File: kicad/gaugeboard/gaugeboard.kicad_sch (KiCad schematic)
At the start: 22 parts, among them J1 LOOM from main board (4-wire 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, J2 HB1 half-bridge #1 (on beam):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, J3 HB2 half-bridge #2 (on beam):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, U1 3.3 V LDO: LP2950-N 3.3 V (TO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, U2 Adafruit ADS122C04 #1 (I2C 0x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, U3 Adafruit ADS122C04 #2 (addres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

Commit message: Gauge board: add pass-through loom output header (J2)
Second 1x4 header wired in parallel with the loom input (GND, +5V, SDA, SCL)
so another I2C board can be daisy-chained. Gauge headers renumbered J3/J4;
docs updated.

Co-Authored-By: Claude Sonnet 5.5 <noreply@anthropic.com>
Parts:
- removed J2: HB1 half-bridge #1 (on beam): V, SIG, GND, Connector_PinHeader_2.54mm:PinHeader_1x03_P2.54mm_Vertical, symbol HastaDAQ:Header1x03_VpSIGpGND
- added J2: LOOM OUT (pass-through, paralleled with J1): GND,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, Connector_PinHeader_2.54mm:PinHeader_1x04_P2.54mm_Vertical, symbol HastaDAQ:Header1x04_GNDp5VpSDApSCL
- added J4: HB2 half-bridge #2 (on beam): V, SIG, GND, Connector_PinHeader_2.54mm:PinHeader_1x03_P2.54mm_Vertical, symbol HastaDAQ:Header1x03_VpSIGpGND
- J3: value HB2 half-bridge #2 (on beam): V, SIG, GND -> HB1 half-bridge #1 (on beam): V, SIG, GND
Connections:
- net +3V3: now also J4.1 (V)
- net +5V: now also J2.2 (5V)
- net ADS1_SIG: now also J3.2 (SIG)
- net ADS2_SIG: now also J4.2 (SIG); no longer J3.2 (SIG)
- net GND: now also J2.1 (GND), J4.3 (GND)
- net SCL: now also J2.4 (SCL)
- net SDA: now also J2.3 (SDA)
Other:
- note added: "Second 1x4 header wired straight to the loom: daisy-chains another I2C board (+5V, 3.3 V logic)."

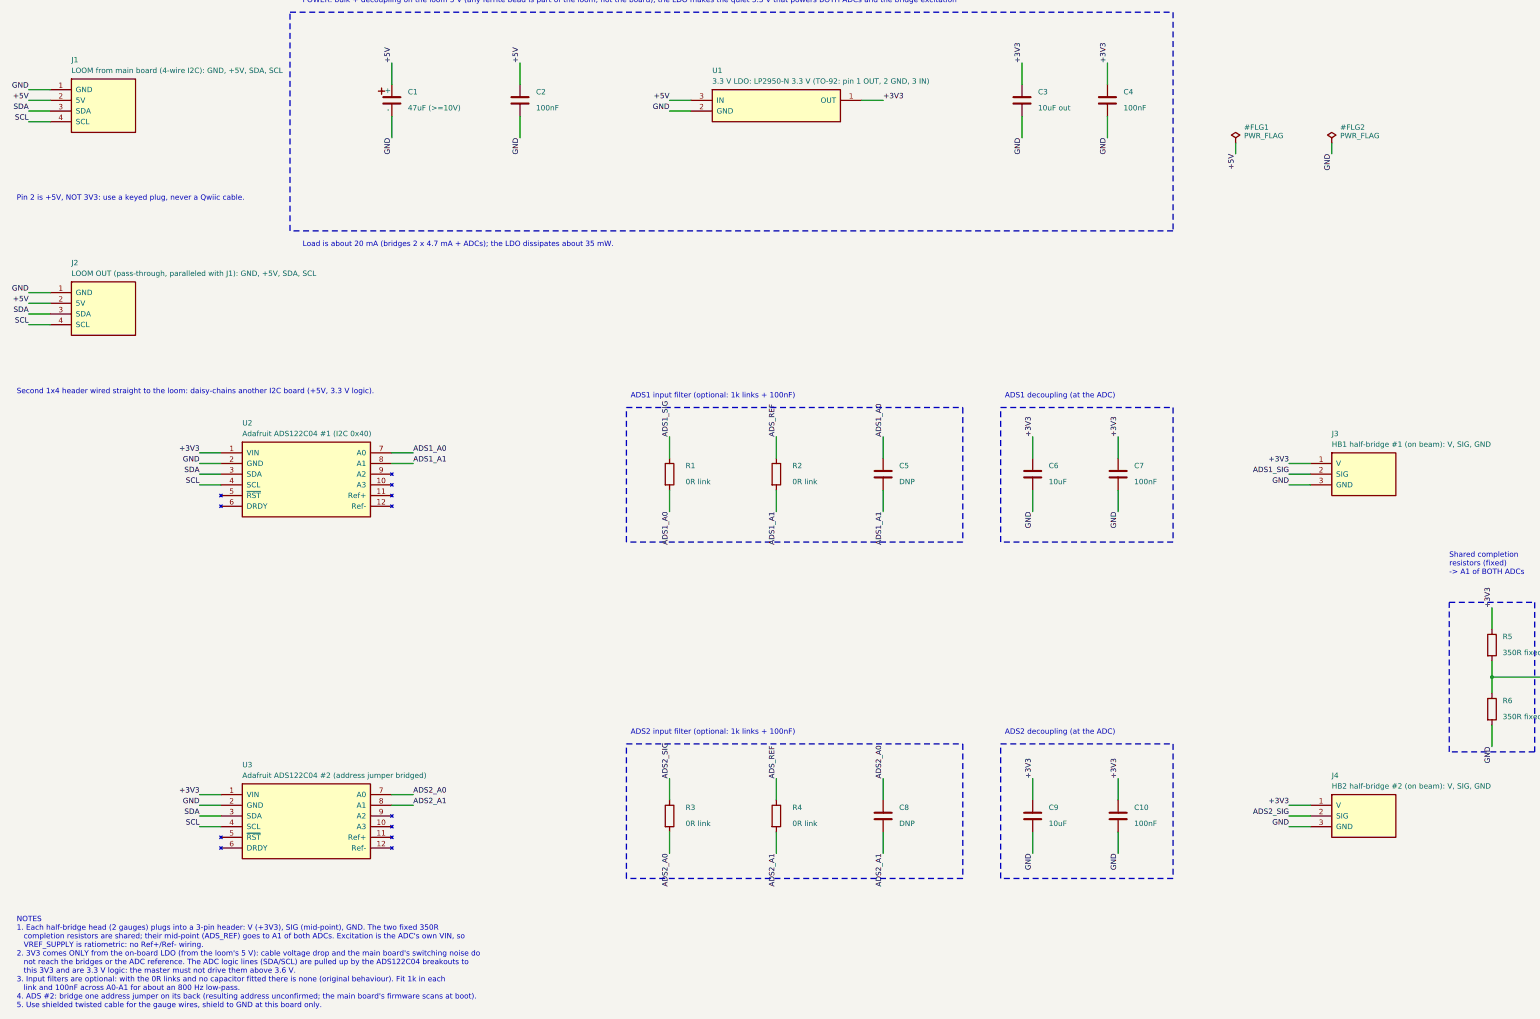
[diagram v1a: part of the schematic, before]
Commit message: Schematics: fuse removed, plain headers, real parts chosen; gauge board LDO/caps; hand-off docs
- Main board: no fuse (+12V straight from the supply connector), every connector a
  plain 0.1 in header, plain test pads, FOD817A opto, chosen capacitor footprints
- Gauge board: MCP1700-3302E/TO LDO (pin 1 GND, 2 VIN, 3 VOUT), tantalum output cap,
  Vishay K-series 100 nF with 2.5 mm pitch, DNP flags on the filter caps, test points,
  pass-through loom header, redundant ADC decoupling removed
- Docs: PCB_BRIEF.md/PCB_BRIEF_GAUGE.md rewritten with a status and hand-off section,
  new PARTS_TO_SELECT.md (RS numbers, dimensions, open items), README updated,
  BabyBuck EN and ADS122C04 pull-up/address facts recorded from the data sheets

Co-Authored-By: Claude Sonnet 5.5 <noreply@anthropic.com>
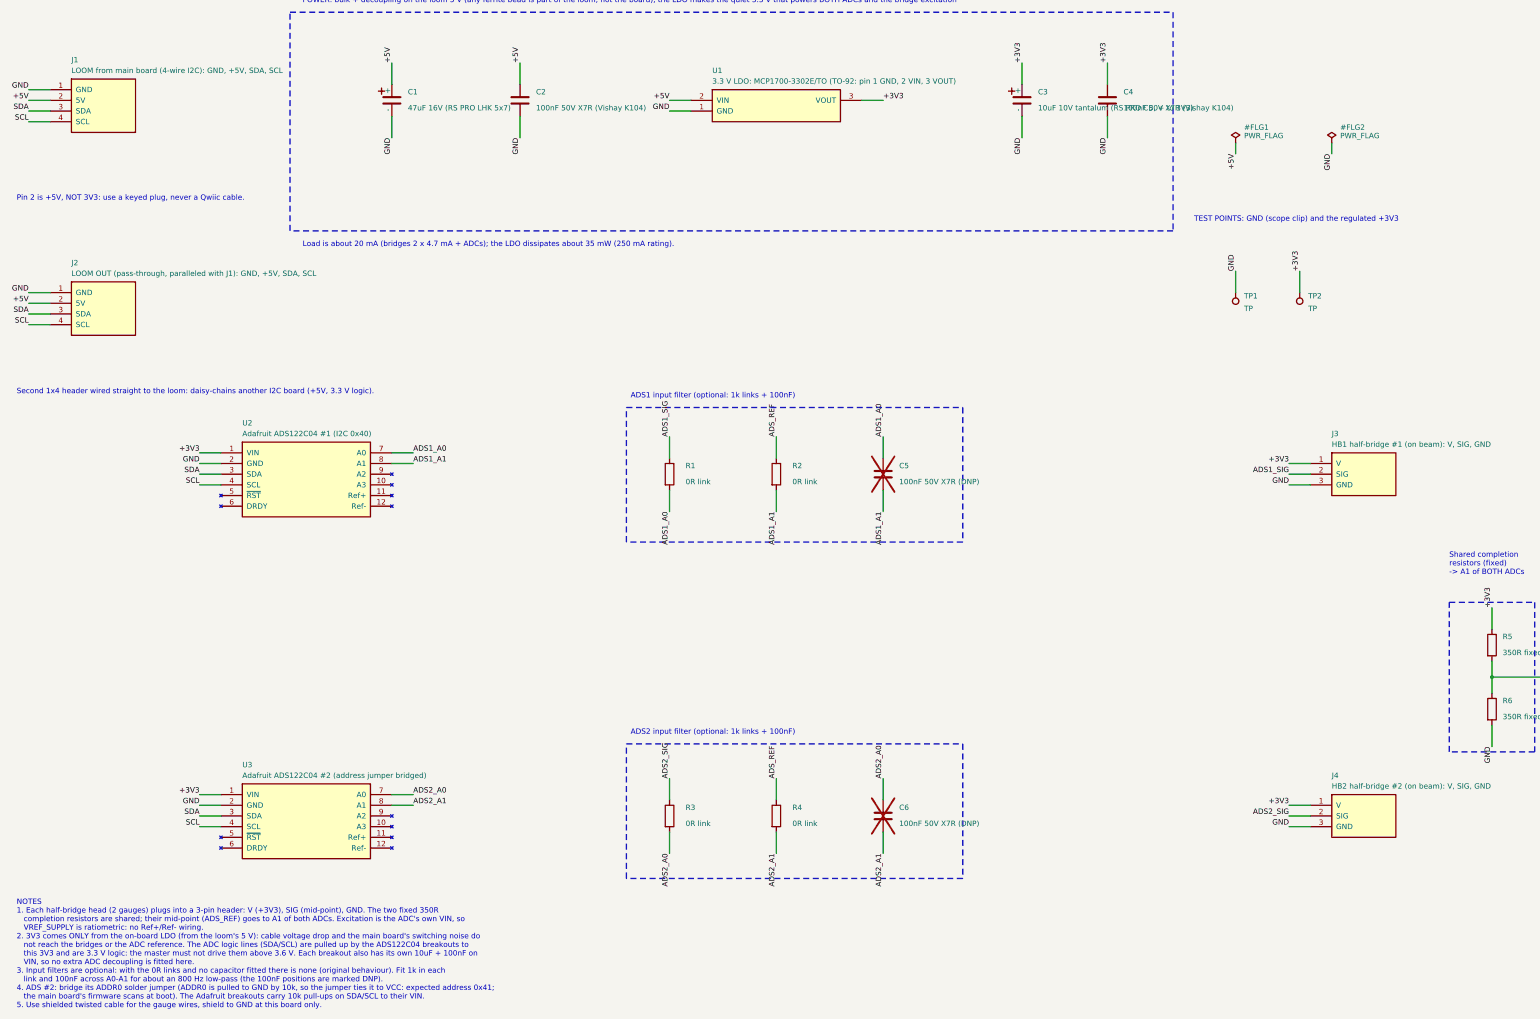
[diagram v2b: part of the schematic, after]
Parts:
- removed C10, C7: 100nF, Capacitor_THT:C_Disc_D5.0mm_W2.5mm_P5.00mm, symbol HastaDAQ:C
- removed C3: 10uF out, Capacitor_THT:C_Rect_L7.2mm_W3.5mm_P5.00mm, symbol HastaDAQ:C
- removed C8: DNP, Capacitor_THT:C_Disc_D5.0mm_W2.5mm_P5.00mm, symbol HastaDAQ:C
- removed C9: 10uF, Capacitor_THT:C_Rect_L7.2mm_W3.5mm_P5.00mm, symbol HastaDAQ:C
- added C3: 10uF 10V tantalum (RS PRO CB, + to 3V3), Capacitor_THT:CP_Radial_D5.0mm_P2.50mm, symbol HastaDAQ:C_Polarized
- added TP1, TP2: TP, TestPoint:TestPoint_Pad_D2.0mm, symbol HastaDAQ:TestPoint
- C1: value 47uF (>=10V) -> 47uF 16V (RS PRO LHK 5x7)
- C2, C4: value 100nF -> 100nF 50V X7R (Vishay K104); footprint Capacitor_THT:C_Disc_D5.0mm_W2.5mm_P5.00mm -> Capacitor_THT:C_Rect_L4.0mm_W2.5mm_P2.50mm
- C5: value DNP -> 100nF 50V X7R (DNP); footprint Capacitor_THT:C_Disc_D5.0mm_W2.5mm_P5.00mm -> Capacitor_THT:C_Rect_L4.0mm_W2.5mm_P2.50mm; now not fitted
- C6: value 10uF -> 100nF 50V X7R (DNP); footprint Capacitor_THT:C_Rect_L7.2mm_W3.5mm_P5.00mm -> Capacitor_THT:C_Rect_L4.0mm_W2.5mm_P2.50mm; now not fitted
- U1: value 3.3 V LDO: LP2950-N 3.3 V (TO-92: pin 1 OUT, 2 GND, 3 IN) -> 3.3 V LDO: MCP1700-3302E/TO (TO-92: pin 1 GND, 2 VIN, 3 VOUT)
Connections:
- net +3V3: now also U1.3 (VOUT), C3.1 (+), TP2.1; no longer C6.1, U1.1 (OUT)
- net +5V: now also U1.2 (VIN); no longer U1.3 (IN)
- net ADS2_A0: now also C6.1
- net ADS2_A1: now also C6.2
- net GND: now also U1.1 (GND), C3.2 (-), TP1.1; no longer C6.2, U1.2 (GND)
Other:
- note added: "Load is about 20 mA (bridges 2 x 4.7 mA + ADCs); the LDO dissipates about 35 mW (250 mA rating)."
- note added: "TEST POINTS: GND (scope clip) and the regulated +3V3"
- note removed: "ADS1 decoupling (at the ADC)"
- note removed: "ADS2 decoupling (at the ADC)"
- note removed: "Load is about 20 mA (bridges 2 x 4.7 mA + ADCs); the LDO dissipates about 35 mW."

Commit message: Gauge board PCB laid out, routed and sent to PCBWay; layout scripts, docs and hand-off README
- Gauge board: J3/J4 become 2x3 headers (V V / SIG SIG / GND GND) in generate_gauge_sch.py;
  republished release 20261026-2252-rev-a (replaces 20261026-1734-rev-a) with the laid-out
  gaugeboard.kicad_pcb and the PCBWay fab files (fab/gaugeboard_gerbers.zip).
- kicad/tools/layout/: export_fab.py, tidy_silk.py, remove_pads.py, set_pcbway_rules.py plus
  board-specific placement/routing/length-check records for the gauge board, with a README.
- kicad/README.md: workflow, tools, gotchas, status, as-built gauge board, next steps for the main board.
- docs: PCB_BRIEF_GAUGE.md updated to the as-built layout, PARTS_TO_SELECT.md and README.md to match.
- Not committed: the nested KiCad .history folder in the release (local editor history).

Co-Authored-By: Claude Sonnet 5.5 <noreply@anthropic.com>
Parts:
- removed J3: HB1 half-bridge #1 (on beam): V, SIG, GND, Connector_PinHeader_2.54mm:PinHeader_1x03_P2.54mm_Vertical, symbol HastaDAQ:Header1x03_VpSIGpGND
- removed J4: HB2 half-bridge #2 (on beam): V, SIG, GND, Connector_PinHeader_2.54mm:PinHeader_1x03_P2.54mm_Vertical, symbol HastaDAQ:Header1x03_VpSIGpGND
- added J3: HB1 half-bridge #1 (on beam), 2x3: V V / SIG SIG 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, Connector_PinHeader_2.54mm:PinHeader_2x03_P2.54mm_Vertical, symbol HastaDAQ:Header2x03_VpVpSIGpSIGpGNDpGND
- added J4: HB2 half-bridge #2 (on beam), 2x3: V V / SIG SIG 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, Connector_PinHeader_2.54mm:PinHeader_2x03_P2.54mm_Vertical, symbol HastaDAQ:Header2x03_VpVpSIGpSIGpGNDpGND
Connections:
- net +3V3: now also J3.1 (V), J3.2 (V), J4.1 (V), J4.2 (V)
- net ADS1_SIG: now also J3.3 (SIG), J3.4 (SIG)
- net ADS2_SIG: now also J4.3 (SIG), J4.4 (SIG)
- net GND: now also J3.5 (GND), J3.6 (GND), J4.5 (GND), J4.6 (GND)
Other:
- note added: "NOTES 1. Each half-bridge head (2 gauges) plugs into a 2x3 header with doubled rows: V V (+3V3) / SIG SIG (mid-point) / GND GND, so two quarter-bridge gauges can be completed into a half bridge in the plug. The two fixed 350R completion resistors are shared; their mid-point (ADS_REF) goes to A1 of both ADCs. Excitation is the ADC's own VIN, so VREF_SUPPLY is ratiometric: no Ref+/Ref- wiring. 2. 3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"
- note removed: "NOTES 1. Each half-bridge head (2 gauges) plugs into a 3-pin header: V (+3V3), SIG (mid-point), GND. The two fixed 350R completion resistors are shared; their mid-point (ADS_REF) goes to A1 of both ADCs. Excitation is the ADC's own VIN, so VREF_SUPPLY is ratiometric: no Ref+/Ref- wiring. 2. 3V3 comes ONLY from the on-board LDO (from the loom's 5 V): cable voltage drop and the main board's switchi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"
